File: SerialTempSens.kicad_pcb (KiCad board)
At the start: 2 copper layers, 60.5 x 25 mm, 35 parts, among them J1 Conn_01x02, J2 Conn_01x02, J3 Conn_01x02, J4 USB_B_Micro, J5 Conn_01x05, SW1 SW_Push, U1 MIC5504-3.3YM5, U2 STM32G0B1KCTx, U3 OLED Display, U4 USBLC6-2SC6

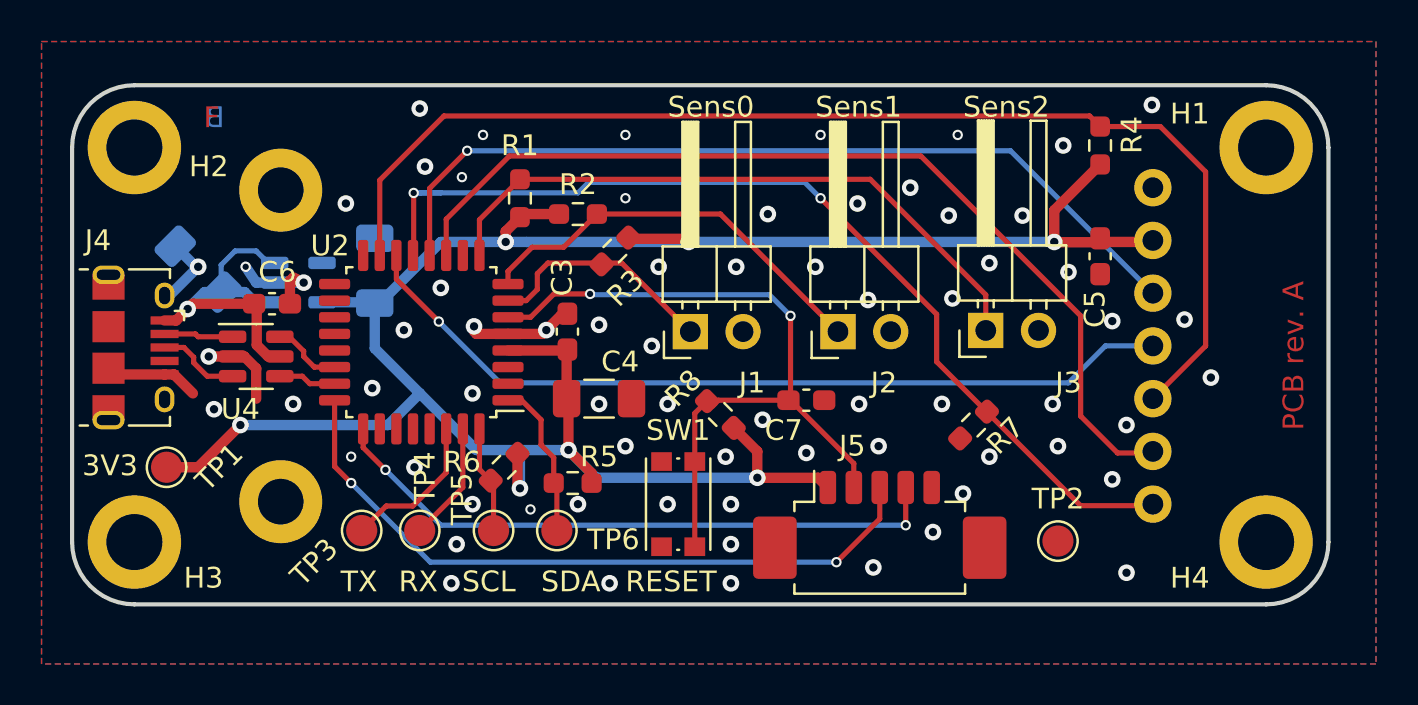
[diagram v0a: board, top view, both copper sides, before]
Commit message: Rename project, update footprint
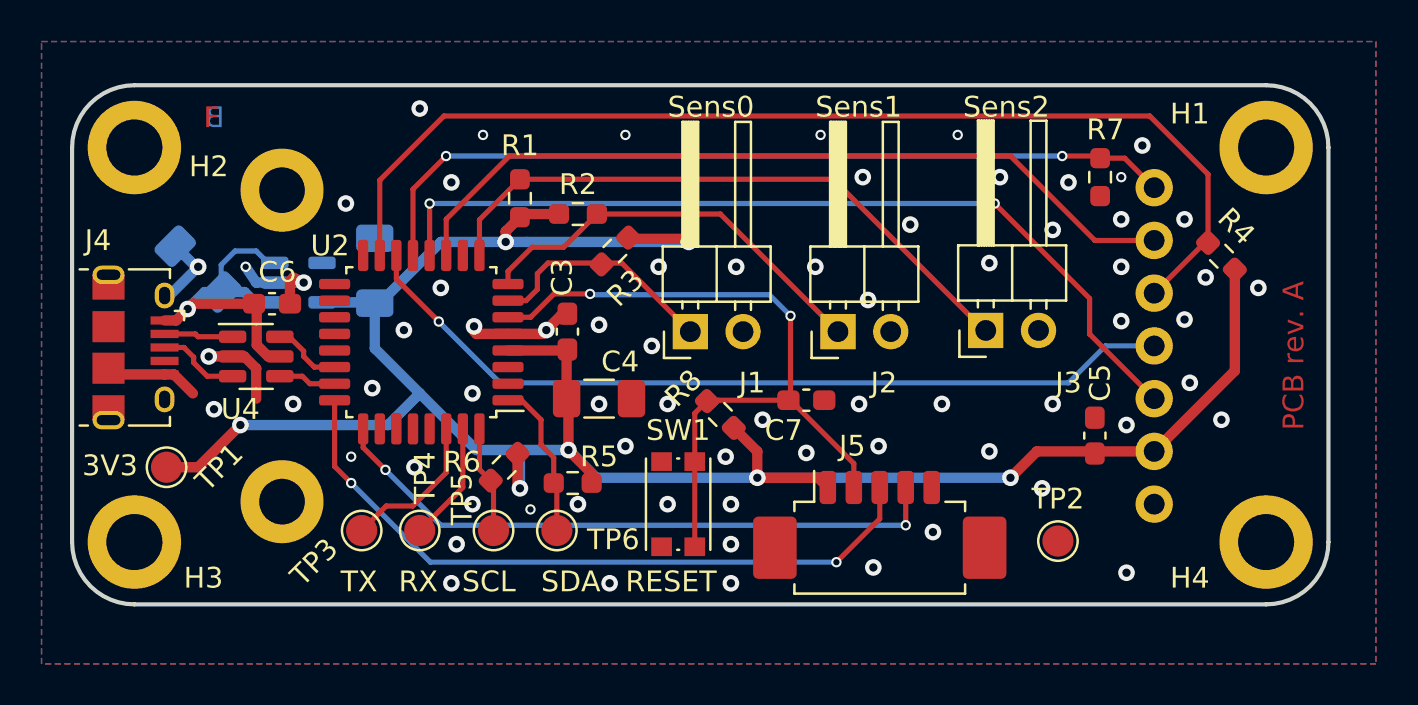
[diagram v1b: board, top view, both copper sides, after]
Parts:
- moved U3 43.8 mm to (106.8, 71.6), turned to 0 degrees
- moved R7 13.4 mm to (148.0, 63.4), turned to -90 degrees
- moved C5 8.64 mm to (147.8, 75.9), turned to 90 degrees
- moved R4 7.91 mm to (153.8, 67.2), turned to 135 degrees
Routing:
- net /DISP_CS: track 47.8 -> 40.2 mm
- net /DISP_DC: track 45.6 -> 38.8 mm
- net /DISP_RST: track 57.8 -> 52.8 mm
- net +3V3: track 107.8 -> 111.0 mm
- net Net-(J3-Pin_1): track 30.9 -> 29.9 mm
- net /SPI1_SCK: track 41.7 -> 42.3 mm, vias 1 -> 2
